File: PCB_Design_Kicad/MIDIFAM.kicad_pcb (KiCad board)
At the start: 2 copper layers, 58 x 87.2 mm, 70 parts, among them IC1 DAC8562SDGSR, J1 PWR_IN, J10 midi, J11 back bottom, J12 front bottom, J13 back top, J14 front top, J2 ISP connector, J3 Voct_A, J4 Trig_A, J5 Vel_A, J6 Voct_B, J7 Trig_B, J8 Vel_B, J9 adv_clock_out, SW1 re-sync, SW2 midi learn, SW3 seq. mode, U2 MCP1703Ax-500xxDB, U4 OPA4196xD, U5 6N137, U6 ATmega328-A

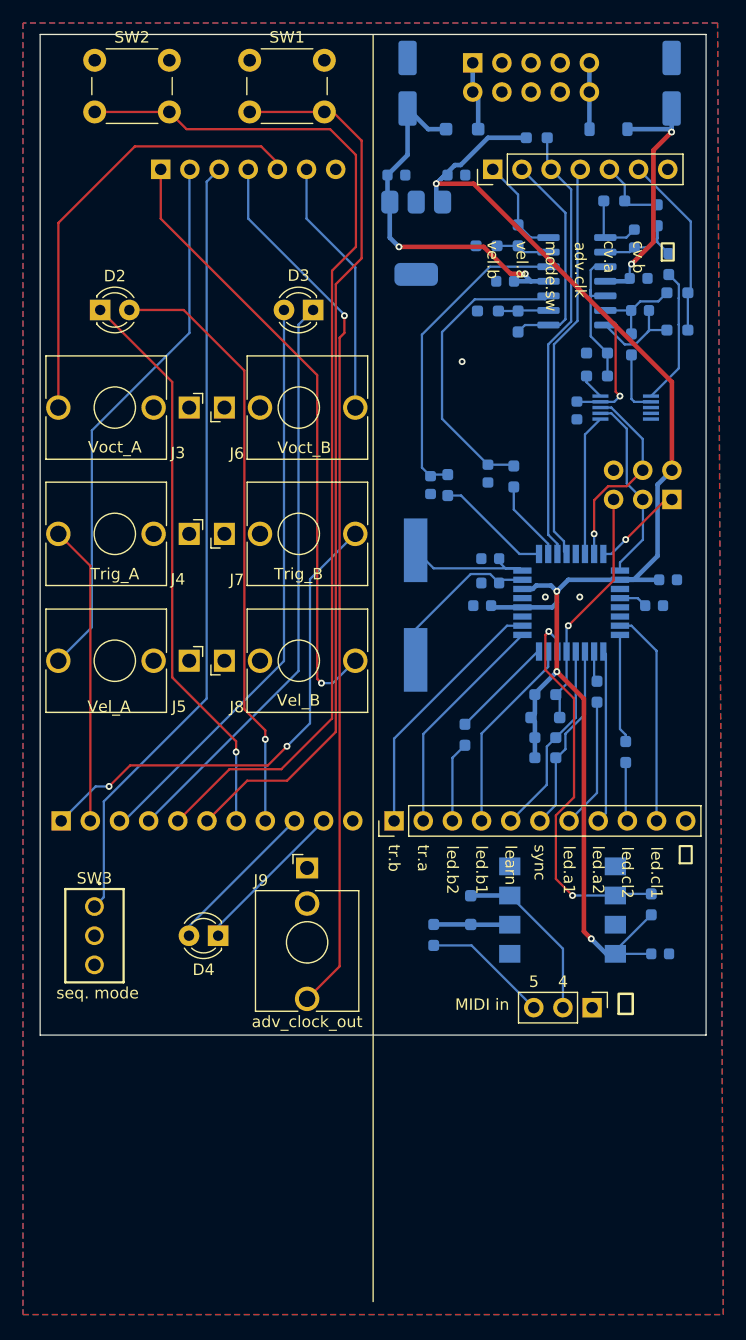
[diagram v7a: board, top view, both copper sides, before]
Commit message: adding to BOM
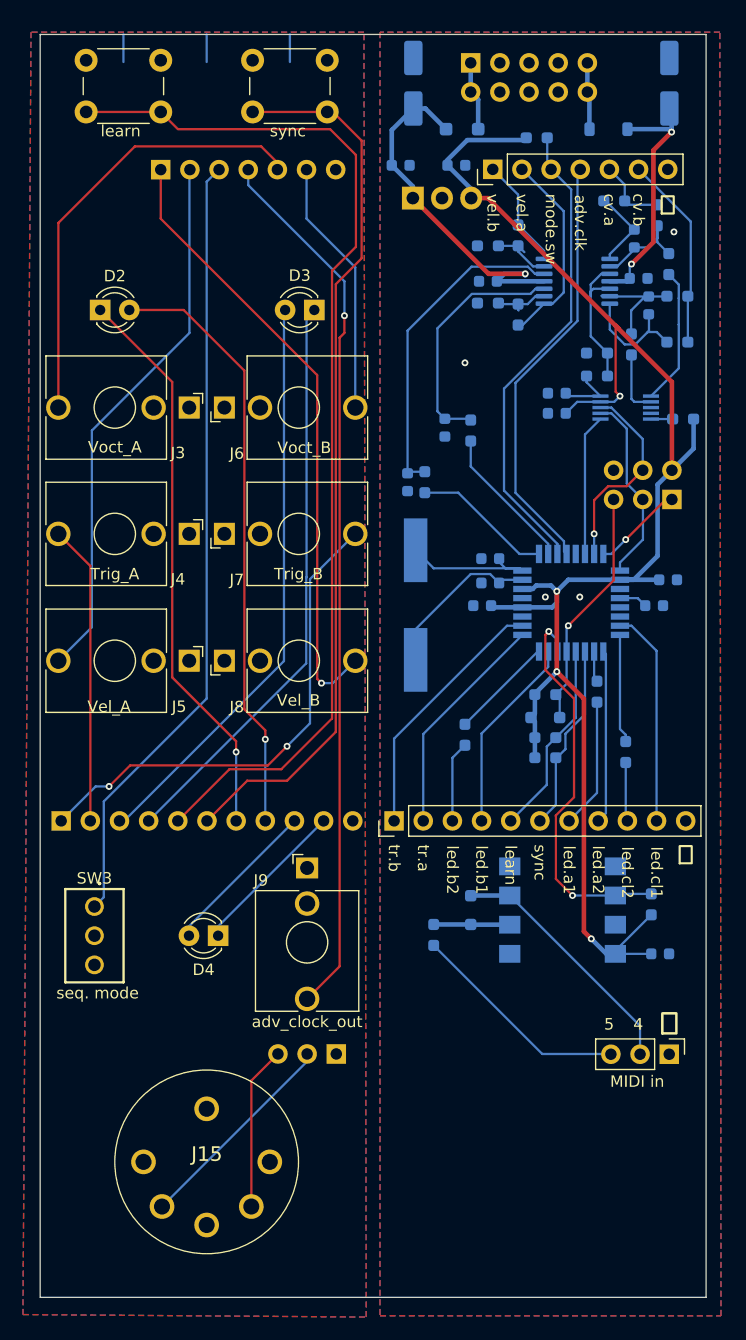
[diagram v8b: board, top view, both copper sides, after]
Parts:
- removed U2: MCP1703Ax-500xxDB, Package_TO_SOT_SMD:SOT-223-3_TabPin2
- added C18: 150n, Capacitor_SMD:C_0603_1608Metric, B.Cu at (99.8, 56.2)
- added J15: SD-50BV, SamacSys_Parts:SD-50BV, F.Cu at (69.3, 123.2)
- added J16: midi, Connector_PinSocket_2.54mm:PinSocket_1x03_P2.54mm_Vertical, B.Cu at (80.6, 113.8)
- added R24: 10k, Resistor_SMD:R_0603_1608Metric_Pad0.98x0.95mm_HandSolder, B.Cu at (110.8, 58.5)
- added U1: LM7805_TO220, Package_TO_SOT_THT:TO-220-3_Vertical, B.Cu at (87.2, 39.3)
- C11, C9: footprint Capacitor_SMD:CP_Elec_5x5.3 -> Capacitor_SMD:CP_Elec_5x5.4
- C13: value 1u -> 0.1u
- C15, C4: value ?? -> 1u
- C8: value 1u -> 0.33u
- U4: footprint Package_SO:SOIC-14_3.9x8.7mm_P1.27mm -> Package_SO:TSSOP-14_4.4x5mm_P0.65mm
- moved J10 7.85 mm to (109.6, 113.8)
- moved C15 5.48 mm to (90.0, 59.2)
- moved R6 5.48 mm to (92.3, 59.5)
- moved C4 2.02 mm to (86.8, 64.0)
- moved R9 2.02 mm to (88.3, 64.0)
- moved C17 1.77 mm to (99.8, 58.0), turned to 180 degrees
- moved C10 1.50 mm to (93.8, 46.5)
- moved R19 1.05 mm to (110.3, 51.8)
- moved C8 0.93 mm to (86.2, 36.4)
- moved C16 0.87 mm to (107.8, 48.6), turned to -90 degrees
- moved C13 0.85 mm to (91.0, 36.4)
- moved SW2 0.75 mm to (58.8, 27.2)
- moved R23 0.69 mm to (93.8, 48.4)
- moved R22 0.60 mm to (96.4, 49.4)
- moved C9 0.50 mm to (87.3, 29.2)
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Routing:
- net Net-(J16-Pin_2): track 0.00 -> 18.5 mm
- net Net-(J16-Pin_3): track 0.00 -> 14.3 mm
- net /midi5: track 11.0 -> 19.4 mm
- net /midi4: track 15.1 -> 21.9 mm
- net /pwm_vel_A: track 7.08 -> 12.6 mm
- net Net-(U4A-+): track 26.1 -> 21.2 mm
- net /seq_mode_sw_b: track 38.3 -> 41.5 mm
- net /VREF_DAC: track 2.25 -> 5.38 mm
- net /adv_clock_b: track 34.9 -> 37.7 mm
- net 5V: track 140.1 -> 142.4 mm, vias 5 -> 4
- net /pwm_vel_b: track 10.1 -> 12.2 mm
- net Net-(C16-Pad2): track 8.50 -> 10.5 mm
- net /CLR_DAC: track 0.00 -> 1.89 mm
- net /vel_a_b: track 19.2 -> 17.4 mm
- net Net-(U4D--): track 8.06 -> 9.43 mm
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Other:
- board size 58 x 87.2 mm -> 58 x 110 mm
- board text added: "V-CUT"
